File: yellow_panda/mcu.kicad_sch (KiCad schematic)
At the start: 22 parts, among them SW65 SW_SPDT, SW66 SW_SPDT, SW67 SW_Push, SW68 SW_Push, U1 STM32F103C8T6, U2 STM32F103C8T6

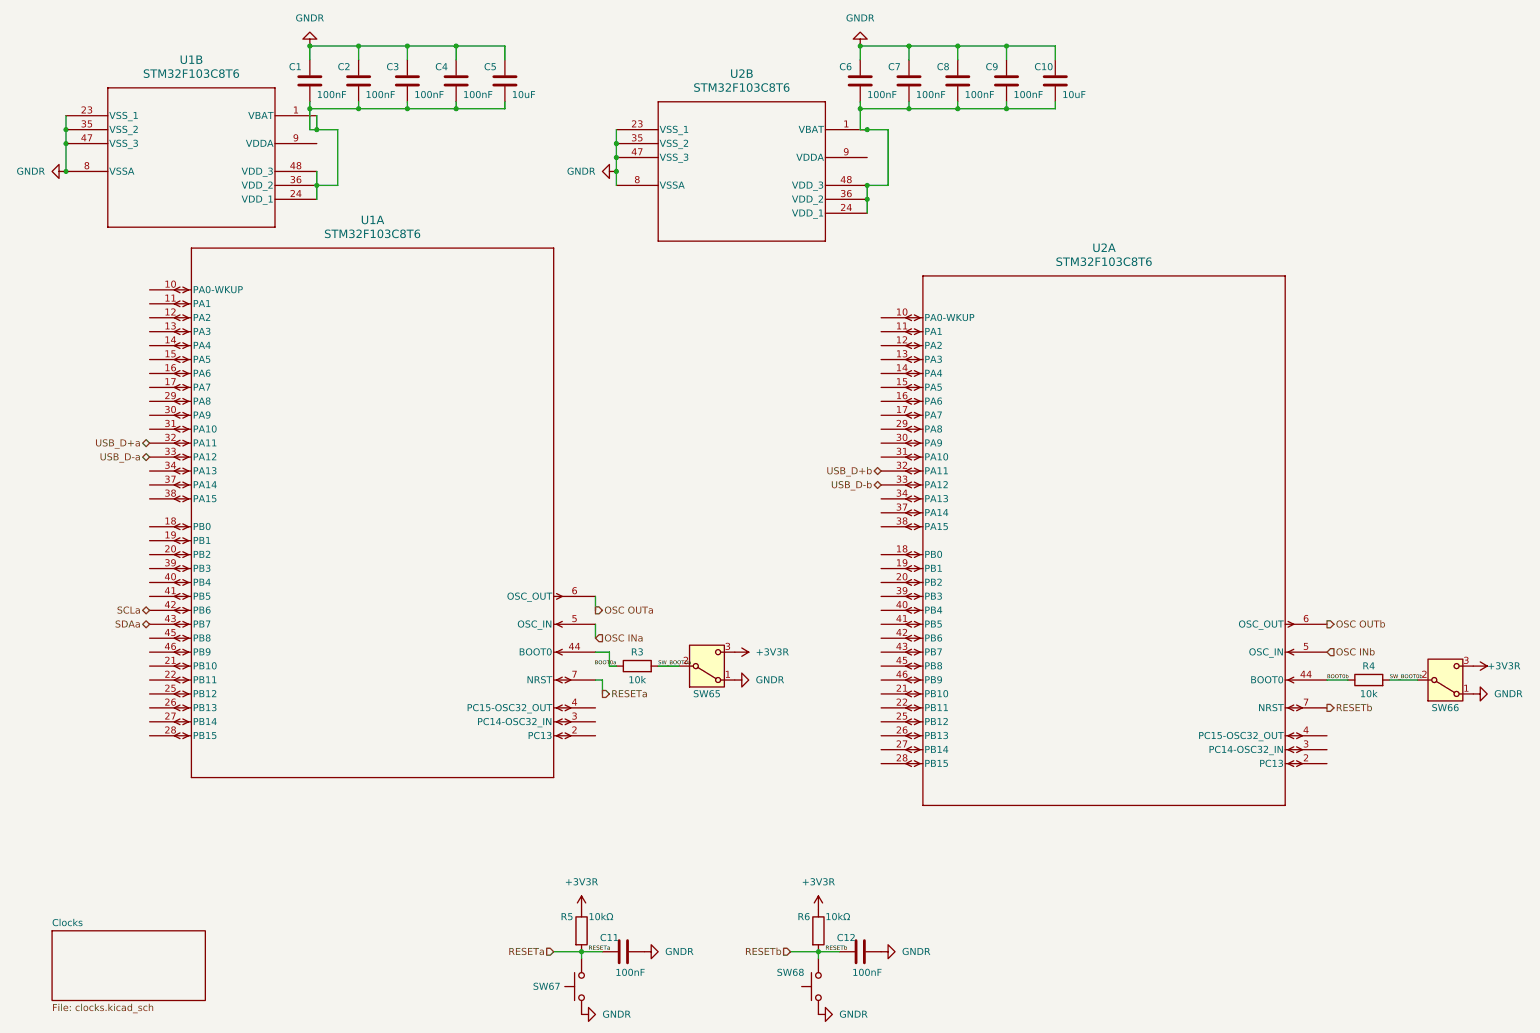
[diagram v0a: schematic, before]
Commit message: Everything is in place now
Swap STM MCU, Correct Switches,
add diodes, caps and resistors
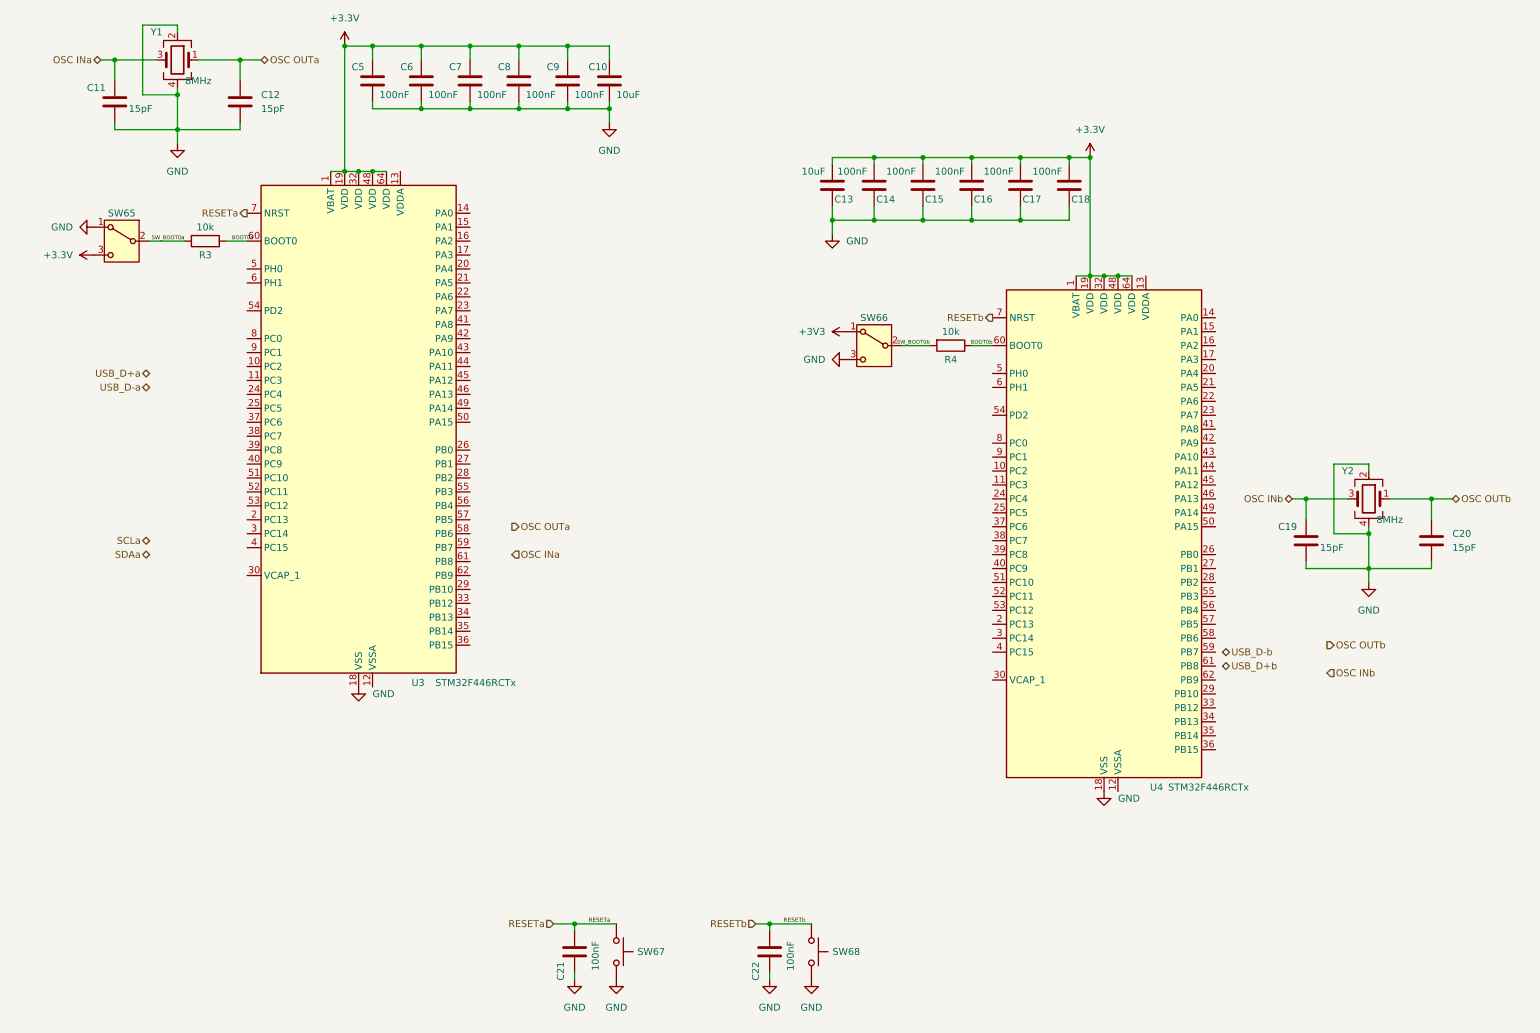
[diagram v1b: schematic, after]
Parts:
- removed C10: 10uF, symbol Device:C
- removed C6, C7, C8: 100nF, symbol Device:C
- removed R5, R6: 10kΩ, symbol Device:R
- removed U1, U2: STM32F103C8T6, STM32F10:LQFP48_STM, symbol stm32F10:STM32F103C8T6
- added C11, C19, C20: 15pF, Capacitor_SMD:C_0402_1005Metric_Pad0.74x0.62mm_HandSolder, symbol Device:C
- added C13: 10uF, Capacitor_SMD:C_1206_3216Metric_Pad1.33x1.80mm_HandSolder, symbol Device:C
- added C14, C15, C16, C17, C18, C22: 100nF, Capacitor_SMD:C_0201_0603Metric_Pad0.64x0.40mm_HandSolder, symbol Device:C
- added U3, U4: STM32F446RCTx, Package_QFP:LQFP-64_10x10mm_P0.5mm, symbol MCU_ST_STM32F4:STM32F446RCTx
- added Y1, Y2: 8MHz, Crystal:Crystal_SMD_Abracon_ABM3B-4Pin_5.0x3.2mm, symbol Device:Crystal_GND24
- C10: renamed from C5; footprint (none) -> Capacitor_SMD:C_1206_3216Metric_Pad1.33x1.80mm_HandSolder
- C12: value 100nF -> 15pF; footprint (none) -> Capacitor_SMD:C_0402_1005Metric_Pad0.74x0.62mm_HandSolder
- C21: renamed from C11; footprint (none) -> Capacitor_SMD:C_0201_0603Metric_Pad0.64x0.40mm_HandSolder
- C5: renamed from C1; footprint (none) -> Capacitor_SMD:C_0201_0603Metric_Pad0.64x0.40mm_HandSolder
- C6: renamed from C2; footprint (none) -> Capacitor_SMD:C_0201_0603Metric_Pad0.64x0.40mm_HandSolder
- C7: renamed from C3; footprint (none) -> Capacitor_SMD:C_0201_0603Metric_Pad0.64x0.40mm_HandSolder
- C8: renamed from C4; footprint (none) -> Capacitor_SMD:C_0201_0603Metric_Pad0.64x0.40mm_HandSolder
- C9: footprint (none) -> Capacitor_SMD:C_0201_0603Metric_Pad0.64x0.40mm_HandSolder
- R3, R4: footprint (none) -> Resistor_SMD:R_0402_1005Metric_Pad0.72x0.64mm_HandSolder
- SW65, SW66: footprint (none) -> Custom Lib:SLW-66527511-SMT-TR_CUD
- SW67, SW68: footprint (none) -> Custom Lib:SW_TL3330_EWI
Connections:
- net BOOT0a: now also U3.60 (BOOT0)
- net BOOT0b: now also U4.60 (BOOT0)
- net OSC INa: now also C11.1, Y1.3
- net OSC INb: now also C19.1, Y2.3
- net OSC OUTa: now also C12.1, Y1.1
- net OSC OUTb: now also C20.1, Y2.1
- net RESETa: now also C21.2, SW67.1, U3.7 (NRST); no longer C21.1, SW67.2
- net RESETb: now also SW68.1, C22.2, U4.7 (NRST); no longer C12.1, SW68.2
- net GND: now reaches C9.2
- net GND: now also C10.2, C12.2, C21.1, C5.2, C6.2, C7.2, C8.2, SW65.1 (A), SW66.3 (C), SW67.2, SW68.2, C11.2, C13.1, C14.1, C15.1, C16.1, C17.1, C18.1, C19.2, C20.2, C22.1, U3.18 (VSS), U3.31 (VSS), U3.47 (VSS), U3.63 (VSS), U4.18 (VSS), U4.31 (VSS), U4.47 (VSS), U4.63 (VSS), Y1.2, Y1.4, Y2.2, Y2.4
- net +3V3R renamed +3.3V
- net +3.3V: now also C10.1, C5.1, C6.1, C7.1, C8.1, C9.1, C13.2, C14.2, C15.2, C16.2, C17.2, C18.2, U3.1 (VBAT), U3.19 (VDD), U3.32 (VDD), U3.48 (VDD), U3.64 (VDD), U4.1 (VBAT), U4.19 (VDD), U4.32 (VDD), U4.48 (VDD), U4.64 (VDD); no longer SW66.3 (C)
- removed net GNDR: C10.1, C12.2, C21.2, C5.1, C6.1, C7.1, C8.1, C9.1, SW65.1 (A), SW66.1 (A), SW67.1, SW68.1
- new net +3V3: SW66.1 (A)
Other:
- removed sheet Clocks
- moved on the sheet: C10, C21, C5, C6, C7, C8, R3, R4, SW65, SW66, SW67

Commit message: rev0.1a - master half done
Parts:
- added C25: 2.2uF, symbol Device:C
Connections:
- net GND: now also C25.1
- net OSC INa: now also U3.5 (PH0)
- net OSC OUTa: now also U3.6 (PH1)
- net SCLa: now also U3.58 (PB6)
- net SDAa: now also U3.59 (PB7)
- net CSa: now reaches U3.20 (PA4)
- net SCKa: now reaches U3.21 (PA5)
- net MISOa: now reaches U3.22 (PA6)
- net MOSIa: now reaches U3.23 (PA7)
- net LCDReseta: now reaches U3.24 (PC4)
- net DataCommanda: now reaches U3.25 (PC5)
- net SDCSa: now reaches U3.26 (PB0)
- net ScreenBrighta: now reaches U3.27 (PB1)
- net Row6a: now reaches U3.28 (PB2)
- net at U3.30 (VCAP_1): now also C25.2
- net ROW5a: now reaches U3.36 (PB15)
- net ROW4a: now reaches U3.37 (PC6)
- net ROW3a: now reaches U3.38 (PC7)
- net ROW2a: now reaches U3.39 (PC8)
- net ROW1a: now reaches U3.40 (PC9)
- net ROW0a: now reaches U3.41 (PA8)
- net UART_TXa: now reaches U3.42 (PA9)
- net UART_RXa: now reaches U3.43 (PA10)
- net USBDa+: now reaches U3.44 (PA11)
- net USBDa-: now reaches U3.45 (PA12)
- net SWDIOa: now reaches U3.46 (PA13)
- net SWCLKa: now reaches U3.49 (PA14)
- net LEDsa: now reaches U3.52 (PC11)
- net COL5a: now reaches U3.53 (PC12)
- net COL4a: now reaches U3.54 (PD2)
- net SWOa: now reaches U3.55 (PB3)
- net COL3a: now reaches U3.56 (PB4)
- net COL2a: now reaches U3.57 (PB5)
- net COL1a: now reaches U3.61 (PB8)
- net COL0a: now reaches U3.62 (PB9)

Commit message: Finished the design
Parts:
- added C28: 2.2uF, Capacitor_SMD:C_0603_1608Metric_Pad1.08x0.95mm_HandSolder, symbol Device:C
- added C29, C30: 100nF, Capacitor_SMD:C_0201_0603Metric_Pad0.64x0.40mm_HandSolder, symbol Device:C
- C25: footprint (none) -> Capacitor_SMD:C_0603_1608Metric_Pad1.08x0.95mm_HandSolder
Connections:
- net +3V3 is gone; now on net +3.3V: SW66.1 (A)
- net +3.3V: now also U3.13 (VDDA), U4.13 (VDDA), C29.1, C30.2
- net GND: now also U3.12 (VSSA), U4.12 (VSSA), C28.1, C29.2, C30.1
- net OSC INb: now also U4.5 (PH0)
- net OSC OUTb: now also U4.6 (PH1)
- net CSb: now reaches U4.20 (PA4)
- net SCKb: now reaches U4.21 (PA5)
- net MISOb: now reaches U4.22 (PA6)
- net MOSIb: now reaches U4.23 (PA7)
- net LCDResetb: now reaches U4.24 (PC4)
- net DataCommandb: now reaches U4.25 (PC5)
- net SDCSb: now reaches U4.26 (PB0)
- net ScreenBrightb: now reaches U4.27 (PB1)
- net LEDsb: now reaches U4.28 (PB2)
- net at U4.30 (VCAP_1): now also C28.2
- net COL0b: now reaches U4.33 (PB12)
- net COL1b: now reaches U4.34 (PB13)
- net COL2b: now reaches U4.35 (PB14)
- net COL3b: now reaches U4.36 (PB15)
- net COL4b: now reaches U4.37 (PC6)
- net COL5b: now reaches U4.38 (PC7)
- net ROW0b: now reaches U4.39 (PC8)
- net ROW1b: now reaches U4.40 (PC9)
- net ROW2b: now reaches U4.41 (PA8)
- net UART_TXb: now reaches U4.42 (PA9)
- net UART_RXb: now reaches U4.43 (PA10)
- net USBDb+: now reaches U4.44 (PA11)
- net USBDb-: now reaches U4.45 (PA12)
- net SWDIOb: now reaches U4.46 (PA13)
- net SWCLKb: now reaches U4.49 (PA14)
- net ROW3b: now reaches U4.50 (PA15)
- net ROW4b: now reaches U4.51 (PC10)
- net ROW5b: now reaches U4.52 (PC11)
- net SWOb: now reaches U4.55 (PB3)
- net SCLb: now reaches U4.58 (PB6)
- net SDAb: now reaches U4.59 (PB7)
- net Row6a: no longer names the net of U3.28 (PB2)
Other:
- moved on the sheet: C19, C20, Y2
